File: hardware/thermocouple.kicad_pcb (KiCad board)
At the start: 2 copper layers, 40 x 30 mm, 34 parts, among them J101 THERM, P1 CON-SENSOR2, P2 DEBUG, P3 BOOT, U1 XMC1XXX24, U102 MAX31856, U103 DRILL, U104 DRILL, U105 DRILL, U106 DRILL

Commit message: Add layout
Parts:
- moved Fiducial_Mark 28.9 mm to (158.1, 128.9)
- moved P3 12.5 mm to (152.8, 148.0), turned to 0 degrees
- moved D1 4.47 mm to (171.8, 151.5), turned to 0 degrees
- moved R101 3.20 mm to (167.5, 150.2), turned to 180 degrees
- moved R1 1.35 mm to (171.8, 150.2), turned to 0 degrees
- moved RP101 0.45 mm to (160.8, 144.5)
- moved C2 0.21 mm to (156.1, 134.6)
- moved P2 0.08 mm to (162.2, 149.2)
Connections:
- U1 pad 13: Net-(U1-Pad13) -> Net-(R1-Pad1)
- U1 pad 7: Net-(R1-Pad1) -> Net-(U1-Pad7)
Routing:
- net VCC: track 6.13 -> 71.5 mm, vias 0 -> 2
- net GND: track 41.3 -> 67.1 mm, vias 17 -> 26
- net Net-(D101-Pad2): track 0.00 -> 15.1 mm, vias 0 -> 2
- net Net-(R1-Pad1): track 0.00 -> 12.6 mm
- net Net-(RP101-Pad1): track 0.00 -> 7.84 mm
- net Net-(RP101-Pad2): track 0.00 -> 7.20 mm
- net Net-(RP101-Pad3): track 0.00 -> 6.55 mm
- net M-CS: track 0.00 -> 5.90 mm, vias 0 -> 2
- net Net-(RP101-Pad4): track 0.00 -> 5.70 mm
- net Net-(P1-Pad4): track 0.00 -> 5.62 mm
- net M-CLK: track 0.00 -> 5.29 mm
- net Net-(P1-Pad5): track 0.00 -> 4.15 mm
- net Net-(P3-Pad2): track 0.00 -> 4.06 mm
- net M-MISO: track 0.00 -> 3.71 mm
- net S-MISO: track 0.00 -> 2.95 mm
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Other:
- net class Default: clearance 0.20066 -> 0.15
- rule trace_clearance: 0.20066 -> 0.15
- rule trace_min: 0.29972 -> 0.2
- rule via_min_size: 0.70104 -> 0.5
- board text added: "status"

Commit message: Minor adujustments
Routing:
- net GND: track 67.1 -> 33.0 mm, vias 26 -> 18
- net (no net): track 24.0 -> 0.00 mm, vias 7 -> 0
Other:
- board text added: "fault"
- board text removed: "Fault"
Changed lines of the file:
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@@
     (links 64)
     (no_connects 0)
-    (area 149.934499 124.734499 190.315501 155.115501)
+    (area 12.679138 124.069999 190.980001 197.065743)
     (thickness 1.6002)
     (drawings 13)
-    (tracks 287)
+    (tracks 255)
     (zones 0)
     (modules 34)
@@
   )
   (setup
-    (last_trace_width 0.25)
+    (last_trace_width 0.29972)
     (user_trace_width 0.2)
     (user_trace_width 0.25)
@@
     (effects (font (size 0.8 0.8) (thickness 0.15)))
   )
-  (gr_text Fault (at 167.515 152.765) (layer F.SilkS)
+  (gr_text fault (at 167.515 152.765) (layer F.SilkS)
     (effects (font (size 0.8 0.8) (thickness 0.14986)))
   )
@@
     (effects (font (size 0.8001 0.8001) (thickness 0.200025)))
   )
-  (segment (start 170.125 126.025) (end 166.125 126.025) (width 0.29972) (layer Rückseite) (net 0))
-  (via (at 158.125 126.025) (size 0.55) (drill 0.25) (layers Vorderseite Rückseite) (net 0))
-  (segment (start 162.125 126.025) (end 158.125 126.025) (width 0.29972) (layer Rückseite) (net 0))
-  (via (at 162.125 126.025) (size 0.55) (drill 0.25) (layers Vorderseite Rückseite) (net 0))
-  (segment (start 163.235 126.025) (end 162.125 126.025) (width 0.29972) (layer Vorderseite) (net 0))
-  (segment (start 166.125 126.025) (end 163.235 126.025) (width 0.29972) (layer Vorderseite) (net 0))
-  (via (at 166.125 126.025) (size 0.55) (drill 0.25) (layers Vorderseite Rückseite) (net 0))
-  (segment (start 170.125 126.025) (end 174.125 126.025) (width 0.29972) (layer Vorderseite) (net 0))
-  (via (at 170.125 126.025) (size 0.55) (drill 0.25) (layers Vorderseite Rückseite) (net 0))
-  (via (at 182.125 126.025) (size 0.55) (drill 0.25) (layers Vorderseite Rückseite) (net 0))
-  (segment (start 182.125 126.025) (end 178.125 126.025) (width 0.29972) (layer Vorderseite) (net 0))
-  (via (at 178.125 126.025) (size 0.55) (drill 0.25) (layers Vorderseite Rückseite) (net 0))
-  (segment (start 174.125 126.025) (end 178.125 126.025) (width 0.29972) (layer Rückseite) (net 0))
-  (via (at 174.125 126.025) (size 0.55) (drill 0.25) (layers Vorderseite Rückseite) (net 0))
   (segment (start 157.375 152.225) (end 157.375 152.955) (width 0.55) (layer Vorderseite) (net 1))
   (via (at 157.375 152.955) (size 0.55) (drill 0.25) (layers Vorderseite Rückseite) (net 1))
@@
   (via (at 166.875 134.075) (size 0.55) (drill 0.25) (layers Vorderseite Rückseite) (net 1))
   (segment (start 166.125 134.0749) (end 166.8749 134.0749) (width 0.59944) (layer Vorderseite) (net 1))
-  (via (at 182.125 153.925) (size 0.55) (drill 0.25) (layers Vorderseite Rückseite) (net 1))
-  (segment (start 170.125 153.925) (end 174.125 153.925) (width 0.29972) (layer Rückseite) (net 1))
-  (segment (start 166.875 150.675) (end 170.125 153.925) (width 0.29972) (layer Rückseite) (net 1))
-  (segment (start 166.8749 145.7251) (end 166.125 145.7251) (width 0.59944) (layer Vorderseite) (net 1))
-  (via (at 166.875 145.725) (size 0.55) (drill 0.25) (layers Vorderseite Rückseite) (net 1))
-  (segment (start 166.8749 145.7251) (end 166.875 145.725) (width 0.59944) (layer Vorderseite) (net 1))
-  (segment (start 166.875 145.725) (end 166.875 150.675) (width 0.29972) (layer Rückseite) (net 1))
-  (via (at 178.125 153.925) (size 0.55) (drill 0.25) (layers Vorderseite Rückseite) (net 1))
-  (segment (start 174.125 153.925) (end 178.125 153.925) (width 0.29972) (layer Vorderseite) (net 1))
-  (via (at 174.125 153.925) (size 0.55) (drill 0.25) (layers Vorderseite Rückseite) (net 1))
-  (segment (start 182.125 153.925) (end 178.125 153.925) (width 0.29972) (layer Rückseite) (net 1))
-  (via (at 158.375 153.925) (size 0.55) (drill 0.25) (layers Vorderseite Rückseite) (net 1))
-  (segment (start 166.125 153.925) (end 170.125 153.925) (width 0.29972) (layer Vorderseite) (net 1))
-  (via (at 170.125 153.925) (size 0.55) (drill 0.25) (layers Vorderseite Rückseite) (net 1))
-  (via (at 162.125 153.925) (size 0.55) (drill 0.25) (layers Vorderseite Rückseite) (net 1))
-  (segment (start 166.125 153.925) (end 162.125 153.925) (width 0.29972) (layer Rückseite) (net 1))
-  (via (at 166.125 153.925) (size 0.55) (drill 0.25) (layers Vorderseite Rückseite) (net 1))
-  (segment (start 158.375 153.925) (end 162.125 153.925) (width 0.29972) (layer Vorderseite) (net 1))
   (segment (start 156.225 151.325) (end 156.225 152.875) (width 0.25) (layer Vorderseite) (net 2))
   (segment (start 157.55318 137.67682) (end 155.925 139.305) (width 0.25) (layer Vorderseite) (net 2))

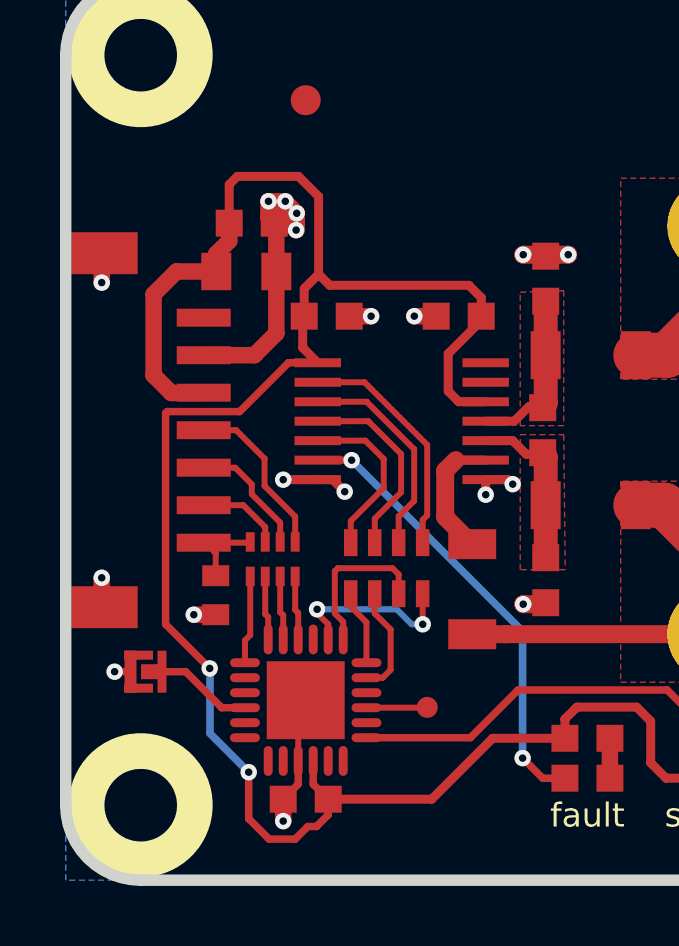
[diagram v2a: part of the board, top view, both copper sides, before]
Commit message: Change VCC route to CoMCU
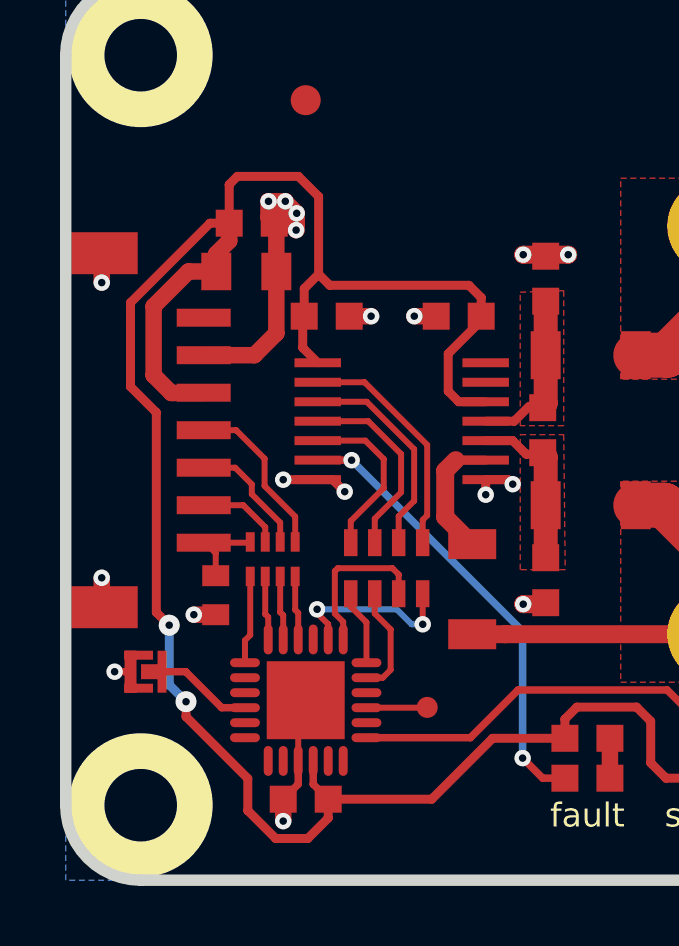
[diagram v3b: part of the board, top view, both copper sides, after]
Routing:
- net VCC: track 71.5 -> 74.0 mm
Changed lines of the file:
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@@
     (thickness 1.6002)
     (drawings 13)
-    (tracks 255)
+    (tracks 256)
     (zones 0)
     (modules 34)
@@
   (via (at 166.875 134.075) (size 0.55) (drill 0.25) (layers Vorderseite Rückseite) (net 1))
   (segment (start 166.125 134.0749) (end 166.8749 134.0749) (width 0.59944) (layer Vorderseite) (net 1))
-  (segment (start 156.225 151.325) (end 156.225 152.875) (width 0.25) (layer Vorderseite) (net 2))
-  (segment (start 157.55318 137.67682) (end 155.925 139.305) (width 0.25) (layer Vorderseite) (net 2))
-  (segment (start 155.925 139.305) (end 153.505 139.305) (width 0.25) (layer Vorderseite) (net 2))
-  (segment (start 153.505 139.305) (end 153.455 139.355) (width 0.25) (layer Vorderseite) (net 2))
-  (segment (start 153.455 139.355) (end 153.455 146.395) (width 0.25) (layer Vorderseite) (net 2))
-  (segment (start 153.455 146.395) (end 154.925 147.865) (width 0.25) (layer Vorderseite) (net 2))
-  (via (at 154.925 147.865) (size 0.55) (drill 0.25) (layers Vorderseite Rückseite) (net 2))
-  (segment (start 154.925 147.865) (end 154.935 147.875) (width 0.25) (layer Rückseite) (net 2))
-  (segment (start 154.935 147.875) (end 154.935 150.035) (width 0.25) (layer Rückseite) (net 2))
-  (segment (start 154.935 150.035) (end 156.225 151.325) (width 0.25) (layer Rückseite) (net 2))
-  (via (at 156.225 151.325) (size 0.55) (drill 0.25) (layers Vorderseite Rückseite) (net 2))
-  (segment (start 158.52592 137.67682) (end 157.55318 137.67682) (width 0.25) (layer Vorderseite) (net 2))
-  (segment (start 158.875 152.745) (end 158.875 152.225) (width 0.25) (layer Vorderseite) (net 2))
-  (segment (start 158.485 153.135) (end 158.875 152.745) (width 0.25) (layer Vorderseite) (net 2))
-  (segment (start 158.195 153.135) (end 158.485 153.135) (width 0.25) (layer Vorderseite) (net 2))
-  (segment (start 157.775 153.555) (end 158.195 153.135) (width 0.25) (layer Vorderseite) (net 2))
-  (segment (start 156.905 153.555) (end 157.775 153.555) (width 0.25) (layer Vorderseite) (net 2))
-  (segment (start 156.225 152.875) (end 156.905 153.555) (width 0.25) (layer Vorderseite) (net 2))
+  (segment (start 152.285 136.395) (end 152.285 135.675) (width 0.29972) (layer Vorderseite) (net 2))
+  (segment (start 154.935 133.025) (end 155.575 133.025) (width 0.29972) (layer Vorderseite) (net 2) (status 800000))
+  (segment (start 152.285 135.675) (end 154.935 133.025) (width 0.29972) (layer Vorderseite) (net 2))
+  (segment (start 158.875 152.225) (end 158.875 152.855) (width 0.29972) (layer Vorderseite) (net 2) (status 400000))
+  (segment (start 152.285 138.475) (end 152.285 136.395) (width 0.29972) (layer Vorderseite) (net 2))
+  (segment (start 153.145 139.335) (end 152.285 138.475) (width 0.29972) (layer Vorderseite) (net 2))
+  (segment (start 153.145 145.995) (end 153.145 139.335) (width 0.29972) (layer Vorderseite) (net 2))
+  (segment (start 153.575 146.425) (end 153.145 145.995) (width 0.29972) (layer Vorderseite) (net 2))
+  (via (at 153.575 146.425) (size 0.70104) (drill 0.24892) (layers Vorderseite Rückseite) (net 2))
+  (segment (start 153.575 148.415) (end 153.575 146.425) (width 0.29972) (layer Rückseite) (net 2))
+  (segment (start 154.135 148.975) (end 153.575 148.415) (width 0.29972) (layer Rückseite) (net 2))
+  (via (at 154.135 148.975) (size 0.70104) (drill 0.24892) (layers Vorderseite Rückseite) (net 2))
+  (segment (start 154.135 149.475) (end 154.135 148.975) (width 0.29972) (layer Vorderseite) (net 2))
+  (segment (start 156.195 151.535) (end 154.135 149.475) (width 0.29972) (layer Vorderseite) (net 2))
+  (segment (start 156.195 152.605) (end 156.195 151.535) (width 0.29972) (layer Vorderseite) (net 2))
+  (segment (start 157.125 153.535) (end 156.195 152.605) (width 0.29972) (layer Vorderseite) (net 2))
+  (segment (start 158.195 153.535) (end 157.125 153.535) (width 0.29972) (layer Vorderseite) (net 2))
+  (segment (start 158.875 152.855) (end 158.195 153.535) (width 0.29972) (layer Vorderseite) (net 2))
   (segment (start 166.765 150.195) (end 166.765 149.555) (width 0.29972) (layer Vorderseite) (net 2))
   (segment (start 170.135 151.525) (end 171.025 151.525) (width 0.29972) (layer Vorderseite) (net 2))
@@
   (segment (start 163.565 135.095) (end 163.975 135.505) (width 0.29972) (layer Vorderseite) (net 2))
   (segment (start 158.925 135.095) (end 163.565 135.095) (width 0.29972) (layer Vorderseite) (net 2))
-  (segment (start 155.575 133.025) (end 155.575 131.735) (width 0.29972) (layer Vorderseite) (net 2))
+  (segment (start 155.575 133.025) (end 155.575 131.755) (width 0.29972) (layer Vorderseite) (net 2))
+  (segment (start 155.575 131.755) (end 155.575 131.735) (width 0.29972) (layer Vorderseite) (net 2))
+  (segment (start 155.575 131.735) (end 155.845 131.465) (width 0.29972) (layer Vorderseite) (net 2))
+  (segment (start 155.845 131.465) (end 157.885 131.465) (width 0.29972) (layer Vorderseite) (net 2))
+  (segment (start 157.885 131.465) (end 158.555 132.135) (width 0.29972) (layer Vorderseite) (net 2))
+  (segment (start 158.555 132.135) (end 158.555 134.725) (width 0.29972) (layer Vorderseite) (net 2))
   (segment (start 158.075 135.205) (end 158.075 136.125) (width 0.29972) (layer Vorderseite) (net 2))
   (segment (start 158.555 134.725) (end 158.075 135.205) (width 0.29972) (layer Vorderseite) (net 2))
-  (segment (start 158.555 132.135) (end 158.555 134.725) (width 0.29972) (layer Vorderseite) (net 2))
-  (segment (start 157.885 131.465) (end 158.555 132.135) (width 0.29972) (layer Vorderseite) (net 2))
-  (segment (start 155.845 131.465) (end 157.885 131.465) (width 0.29972) (layer Vorderseite) (net 2))
-  (segment (start 155.575 131.735) (end 155.845 131.465) (width 0.29972) (layer Vorderseite) (net 2))
   (segment (start 155.14424 134.635) (end 155.14424 134.04576) (width 0.55) (layer Vorderseite) (net 2))
   (segment (start 155.14424 134.04576) (end 155.575 133.615) (width 0.55) (layer Vorderseite) (net 2))
   (segment (start 155.575 133.615) (end 155.575 133.025) (width 0.55) (layer Vorderseite) (net 2))
   (segment (start 154.775 138.685) (end 153.645 138.685) (width 0.55) (layer Vorderseite) (net 2))
-  (segment (start 153.815 134.635) (end 155.14424 134.635) (width 0.55) (layer Vorderseite) (net 2))
-  (segment (start 153.055 135.395) (end 153.815 134.635) (width 0.55) (layer Vorderseite) (net 2))
-  (segment (start 153.055 138.095) (end 153.055 135.395) (width 0.55) (layer Vorderseite) (net 2))
+  (segment (start 154.215 134.635) (end 155.14424 134.635) (width 0.55) (layer Vorderseite) (net 2) (status 800000))
+  (segment (start 153.055 135.795) (end 154.215 134.635) (width 0.55) (layer Vorderseite) (net 2))
+  (segment (start 153.055 138.095) (end 153.055 135.795) (width 0.55) (layer Vorderseite) (net 2))
   (segment (start 153.645 138.685) (end 153.055 138.095) (width 0.55) (layer Vorderseite) (net 2))
   (segment (start 158.0249 137.1758) (end 158.52592 137.67682) (width 0.29972) (layer Vorderseite) (net 2))

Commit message: Add CoMCU logo
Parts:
- added G***: LOGO, kicad-libraries:Logo_CoMCU, B.Cu at (185.3, 139.9)

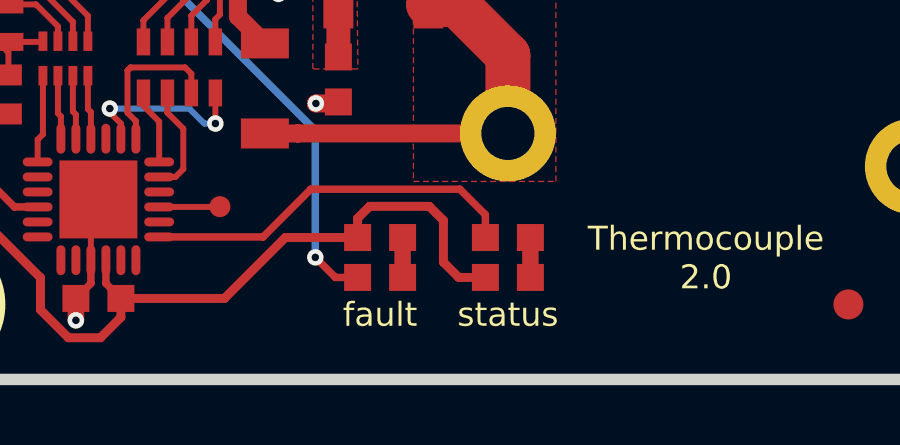
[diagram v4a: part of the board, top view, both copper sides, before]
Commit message: fix text size
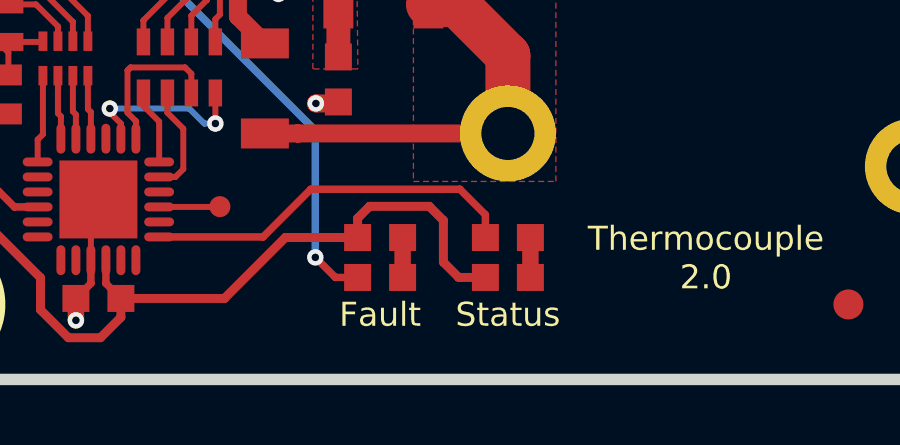
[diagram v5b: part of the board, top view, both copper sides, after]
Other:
- board text added: "Fault"
- board text added: "Status"
- board text removed: "fault"
- board text removed: "status"
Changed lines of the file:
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@@
-(kicad_pcb (version 4) (host pcbnew 4.0.2+dfsg1-stable)
+(kicad_pcb (version 4) (host pcbnew 4.0.7-e2-6376~58~ubuntu17.04.1)
   (general
     (links 64)
     (no_connects 0)
-    (area 149.934499 124.734499 190.315501 155.115501)
+    (area 12.77915 124.069999 190.980001 197.465793)
     (thickness 1.6002)
     (drawings 13)
@@
       (xy 1.301301 2.715081) (xy 1.302426 2.714986)) (layer B.SilkS) (width 0.01))
   )
-  (gr_text status (at 171.775 152.765) (layer F.SilkS)
+  (gr_text Status (at 171.775 152.765) (layer F.SilkS)
     (effects (font (size 0.8 0.8) (thickness 0.14986)))
   )
@@
     (effects (font (size 0.8 0.8) (thickness 0.15)))
   )
-  (gr_text fault (at 167.515 152.765) (layer F.SilkS)
+  (gr_text Fault (at 167.515 152.765) (layer F.SilkS)
     (effects (font (size 0.8 0.8) (thickness 0.14986)))
   )

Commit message: fix logo positions
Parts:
- moved G*** 5.16 mm to (180.1, 139.9)
- moved G*** 5.00 mm to (170.1, 139.9)
- moved VAL 5.00 mm to (160.1, 139.9)
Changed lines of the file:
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@@
   )
   (module kicad-libraries:CE_5mm (layer Rückseite)
-    (at 165.125 139.925 180)
+    (at 160.125 139.925 180)
     (fp_text reference VAL (at 0 0 180) (layer B.SilkS) hide
       (effects (font (size 0.2 0.2) (thickness 0.05)) (justify mirror))
@@
   )
   (module kicad-libraries:WEEE_7mm (layer Rückseite)
-    (at 175.125 139.925 180)
+    (at 170.125 139.925 180)
     (fp_text reference G*** (at 0 0 180) (layer B.SilkS) hide
       (effects (font (size 0.2 0.2) (thickness 0.05)) (justify mirror))
@@
   )
   (module kicad-libraries:Logo_CoMCU (layer Rückseite)
-    (at 185.285 139.865 180)
+    (at 180.125 139.925 180)
     (fp_text reference G*** (at 0 0 180) (layer B.SilkS) hide
       (effects (font (thickness 0.3)) (justify mirror))

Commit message: specify processor
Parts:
- U1: value XMC1XXX24 -> XMC1100
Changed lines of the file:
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@@
       (effects (font (size 0.3 0.3) (thickness 0.075)))
     )
-    (fp_text value XMC1XXX24 (at 0 0.8) (layer F.Fab)
+    (fp_text value XMC1100 (at 0 0.8) (layer F.Fab)
       (effects (font (size 0.3 0.3) (thickness 0.075)))
     )
